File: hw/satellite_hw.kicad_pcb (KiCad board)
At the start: 2 copper layers, 17 parts, among them Q1 2N7002, U1 AP3015, U2 ATtiny13-20SU

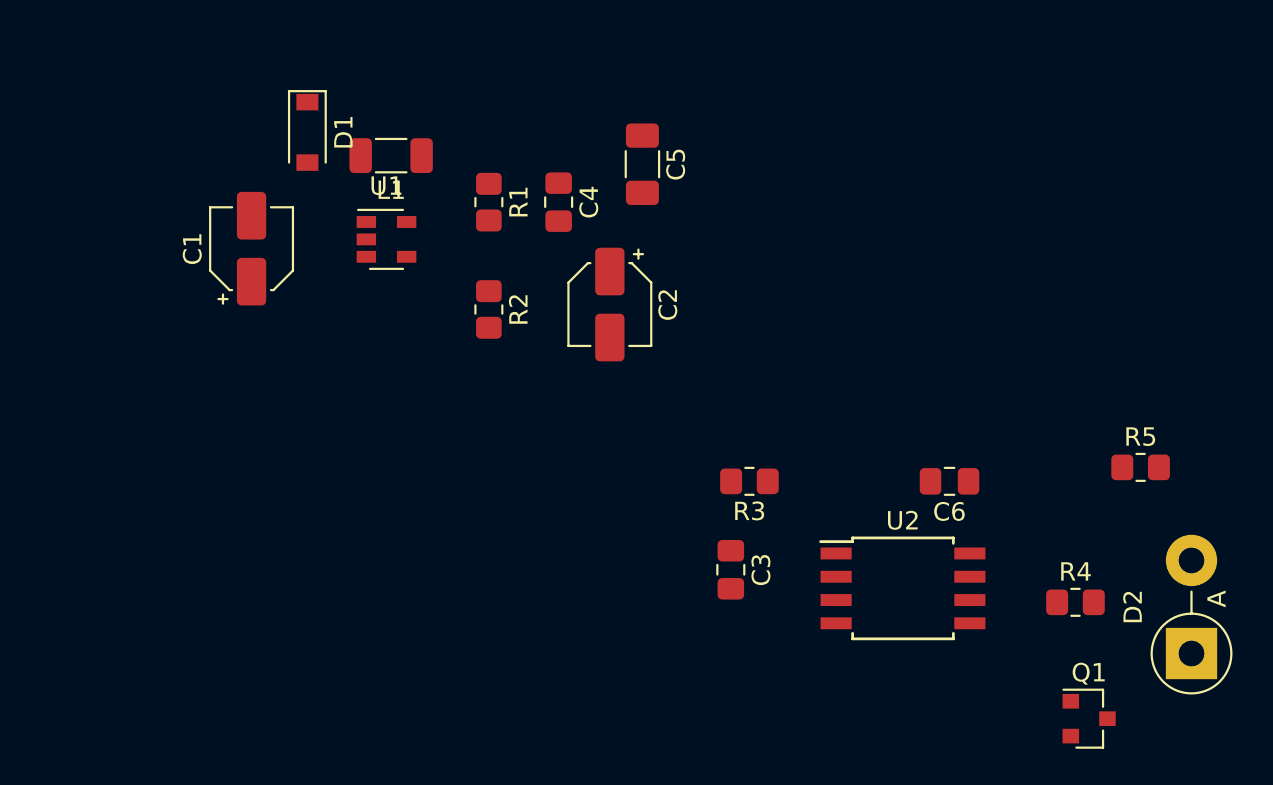
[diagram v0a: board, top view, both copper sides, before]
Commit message: PCB elements alignment + board ground layers
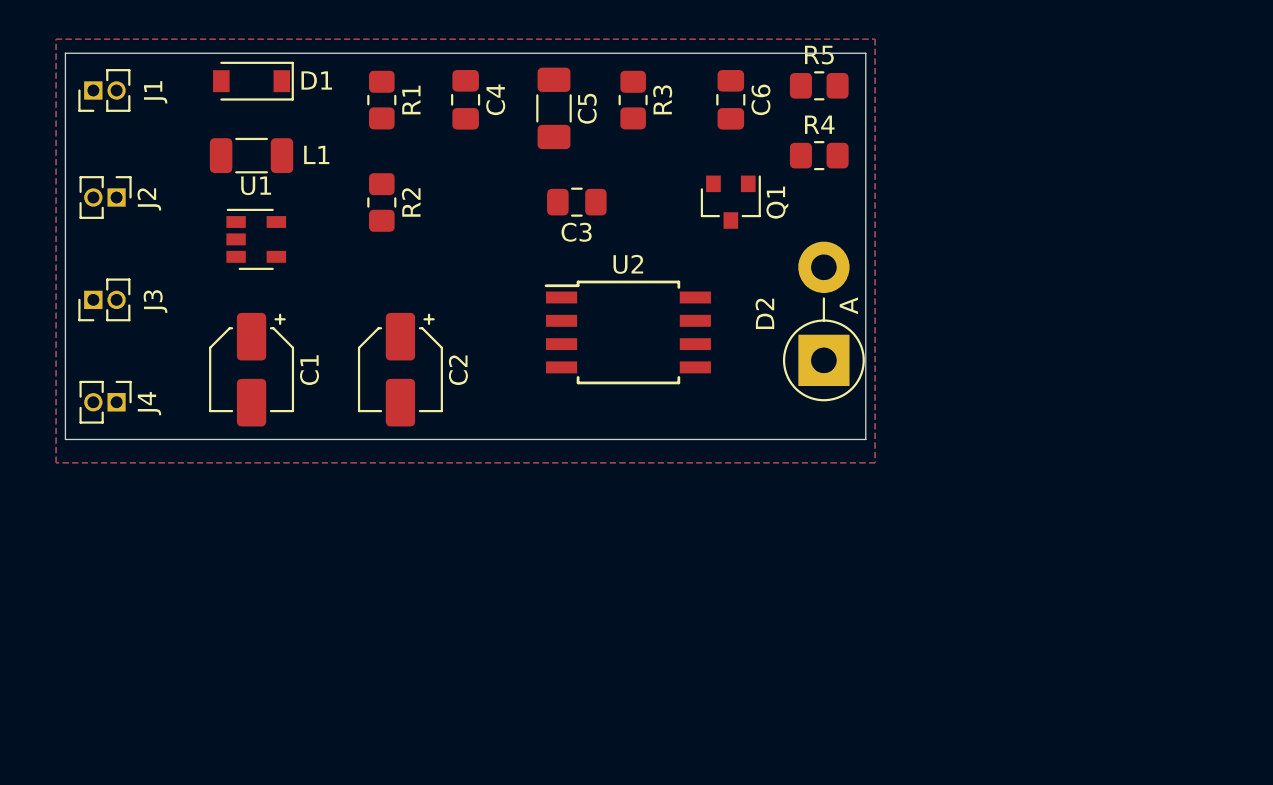
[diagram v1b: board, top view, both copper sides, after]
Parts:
- added J1: solar 1, Connector_PinHeader_1.27mm:PinHeader_1x02_P1.27mm_Vertical, F.Cu at (96.0, 74.7)
- added J2: solar 2, Connector_PinHeader_1.27mm:PinHeader_1x02_P1.27mm_Vertical, F.Cu at (97.3, 80.5)
- added J3: solar 3, Connector_PinHeader_1.27mm:PinHeader_1x02_P1.27mm_Vertical, F.Cu at (96.0, 86.1)
- added J4: solar 4, Connector_PinHeader_1.27mm:PinHeader_1x02_P1.27mm_Vertical, F.Cu at (97.3, 91.7)
- moved Q1 34.3 mm to (130.8, 80.8), turned to 270 degrees
- moved R4 28.1 mm to (135.6, 78.2)
- moved R5 27.2 mm to (135.6, 74.4)
- moved D2 25.7 mm to (135.9, 89.4)
- moved C6 24.0 mm to (130.8, 75.2), turned to 270 degrees
- moved R3 21.8 mm to (125.5, 75.2), turned to 270 degrees
- moved C3 21.8 mm to (122.4, 80.8), turned to 180 degrees
- moved U2 20.5 mm to (125.2, 87.9)
- moved C2 12.0 mm to (112.8, 89.9)
- moved R2 8.26 mm to (111.8, 80.8)
- moved R1 8.07 mm to (111.8, 75.2)
- moved L1 7.62 mm to (104.6, 78.2)
- moved C4 7.55 mm to (116.3, 75.2)
- moved U1 7.11 mm to (104.9, 82.8)
- moved C1 6.60 mm to (104.6, 89.9), turned to 270 degrees
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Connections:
- U2 pad 3: Net-(Q1-Pad1) -> Net-(U2-Pad3)
- U2 pad 6: Net-(U2-Pad6) -> Net-(Q1-Pad1)
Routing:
- added copper zone on B.Cu, net GNDD
- added copper zone on F.Cu, net GNDD
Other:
- board outline added: 43.7 x 21.1 mm

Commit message: removed bottom layer
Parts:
- moved C6 0.80 mm to (130.0, 75.4)
- moved Q1 0.36 mm to (130.6, 81.0), turned to 90 degrees
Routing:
- net +5V: track 0.00 -> 63.5 mm
- net Net-(C4-Pad2): track 0.00 -> 30.8 mm
- net VCC: track 0.00 -> 24.2 mm
- net Net-(Q1-Pad1): track 0.00 -> 21.5 mm
- net Net-(D2-Pad1): track 0.00 -> 13.3 mm
- net Net-(C3-Pad1): track 0.00 -> 11.4 mm
- net Net-(D2-Pad2): track 0.00 -> 11.2 mm
- net Net-(D1-Pad2): track 0.00 -> 8.03 mm
- net Net-(J1-Pad1): track 0.00 -> 5.84 mm
- net Net-(J3-Pad1): track 0.00 -> 5.59 mm
- net Net-(J2-Pad1): track 0.00 -> 5.59 mm
- net GNDD: track 0.00 -> 1.69 mm
- removed copper zone on B.Cu, net GNDD
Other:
- board text added: "+"
- board text added: "-"
- board text added: "toy satellite v0.1"

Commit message: fixed holdpin size
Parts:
- D2: footprint Diode_THT:D_5W_P5.08mm_Vertical_AnodeUp -> LED_THT:LED_D5.0mm-3
- J1, J2, J3, J4: footprint Connector_PinHeader_1.27mm:PinHeader_1x02_P1.27mm_Vertical -> Connector_PinHeader_2.00mm:PinHeader_1x02_P2.00mm_Vertical
- moved J2 0.76 mm to (98.0, 80.5)
- moved J4 0.76 mm to (98.0, 91.7)
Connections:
- U2 pad 2: Net-(U2-Pad2) -> (no net)
- U2 pad 3: Net-(U2-Pad3) -> (no net)
- U2 pad 5: Net-(U2-Pad5) -> (no net)
- U2 pad 7: Net-(U2-Pad7) -> (no net)
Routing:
- net VCC: track 24.2 -> 23.4 mm

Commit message: fixed THT LED size and pins
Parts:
- D2: footprint LED_THT:LED_D5.0mm-3 -> LED_THT:LED_D3.0mm
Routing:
- net Net-(D2-Pad2): track 11.2 -> 14.0 mm
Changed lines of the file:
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@@
     (thickness 1.6)
     (drawings 7)
-    (tracks 88)
+    (tracks 90)
     (zones 0)
     (modules 21)
@@
     (add_net VCC)
   )
+  (module LED_THT:LED_D3.0mm (layer F.Cu)
+    (at 135.89 89.408 90)
+    (descr "LED, diameter 3.0mm, 2 pins")
+    (tags "LED diameter 3.0mm 2 pins")
+    (fp_text reference D2 (at 1.27 -2.96 90) (layer F.SilkS)
+      (effects (font (size 1 1) (thickness 0.15)))
+    )
+    (fp_text value red (at 1.27 2.96 90) (layer F.Fab)
+      (effects (font (size 1 1) (thickness 0.15)))
+    )
+    (fp_arc (start 1.27 0) (end 0.229039 1.08) (angle -87.9) (layer F.SilkS) (width 0.12))
+    (fp_arc (start 1.27 0) (end 0.229039 -1.08) (angle 87.9) (layer F.SilkS) (width 0.12))
+    (fp_arc (start 1.27 0) (end -0.29 1.235516) (angle -108.8) (layer F.SilkS) (width 0.12))
+    (fp_arc (start 1.27 0) (end -0.29 -1.235516) (angle 108.8) (layer F.SilkS) (width 0.12))
+    (fp_arc (start 1.27 0) (end -0.23 -1.16619) (angle 284.3) (layer F.Fab) (width 0.1))
+    (fp_circle (center 1.27 0) (end 2.77 0) (layer F.Fab) (width 0.1))
+    (fp_line (start -0.23 -1.16619) (end -0.23 1.16619) (layer F.Fab) (width 0.1))
+    (fp_line (start -0.29 -1.236) (end -0.29 -1.08) (layer F.SilkS) (width 0.12))
+    (fp_line (start -0.29 1.08) (end -0.29 1.236) (layer F.SilkS) (width 0.12))
+    (fp_line (start -1.15 -2.25) (end -1.15 2.25) (layer F.CrtYd) (width 0.05))
+    (fp_line (start -1.15 2.25) (end 3.7 2.25) (layer F.CrtYd) (width 0.05))
+    (fp_line (start 3.7 2.25) (end 3.7 -2.25) (layer F.CrtYd) (width 0.05))
+    (fp_line (start 3.7 -2.25) (end -1.15 -2.25) (layer F.CrtYd) (width 0.05))
+    (pad 2 thru_hole circle (at 2.54 0 90) (size 1.8 1.8) (drill 0.9) (layers *.Cu *.Mask)
+      (net 8 "Net-(D2-Pad2)"))
+    (pad 1 thru_hole rect (at 0 0 90) (size 1.8 1.8) (drill 0.9) (layers *.Cu *.Mask)
+      (net 7 "Net-(D2-Pad1)"))
+    (model ${KISYS3DMOD}/LED_THT.3dshapes/LED_D3.0mm.wrl
+      (at (xyz 0 0 0))
+      (scale (xyz 1 1 1))
+      (rotate (xyz 0 0 0))
+    )
+  )
   (module Connector_PinHeader_2.00mm:PinHeader_1x02_P2.00mm_Vertical (layer F.Cu)
     (at 98.044 91.694 270)
@@
       (net 7 "Net-(D2-Pad1)"))
     (model ${KISYS3DMOD}/Package_TO_SOT_SMD.3dshapes/SOT-23.wrl
-      (at (xyz 0 0 0))
-      (scale (xyz 1 1 1))
-      (rotate (xyz 0 0 0))
-    )
-  )
-  (module LED_THT:LED_D5.0mm-3 (layer F.Cu)
-    (at 135.89 89.408 90)
-    (descr "LED, diameter 5.0mm, 2 pins, diameter 5.0mm, 3 pins, http://www.kingbright.com/attachments/file/psearch/000/00/00/L-59EGC(Ver.17A).pdf")
-    (tags "LED diameter 5.0mm 2 pins diameter 5.0mm 3 pins")
-    (fp_text reference D2 (at 2.54 -3.96 90) (layer F.SilkS)
-      (effects (font (size 1 1) (thickness 0.15)))
-    )
-    (fp_text value red (at 2.54 3.96 90) (layer F.Fab)
-      (effects (font (size 1 1) (thickness 0.15)))
-    )
-    (fp_line (start 6.25 -3.25) (end -1.15 -3.25) (layer F.CrtYd) (width 0.05))
-    (fp_line (start 6.25 3.25) (end 6.25 -3.25) (layer F.CrtYd) (width 0.05))
-    (fp_line (start -1.15 3.25) (end 6.25 3.25) (layer F.CrtYd) (width 0.05))
-    (fp_line (start -1.15 -3.25) (end -1.15 3.25) (layer F.CrtYd) (width 0.05))
-    (fp_line (start -0.02 1.08) (end -0.02 1.545) (layer F.SilkS) (width 0.12))
-    (fp_line (start -0.02 -1.545) (end -0.02 -1.08) (layer F.SilkS) (width 0.12))
-    (fp_line (start 0.04 -1.469694) (end 0.04 1.469694) (layer F.Fab) (width 0.1))
-    (fp_circle (center 2.54 0) (end 5.04 0) (layer F.Fab) (width 0.1))
-    (fp_arc (start 2.54 0) (end 0.04 -1.469694) (angle 299.1) (layer F.Fab) (width 0.1))
-    (fp_arc (start 2.54 0) (end -0.02 -1.54483) (angle 127.7) (layer F.SilkS) (width 0.12))
-    (fp_arc (start 2.54 0) (end -0.02 1.54483) (angle -127.7) (layer F.SilkS) (width 0.12))
-    (fp_arc (start 2.54 0) (end 0.285316 -1.08) (angle 128.8) (layer F.SilkS) (width 0.12))
-    (fp_arc (start 2.54 0) (end 0.285316 1.08) (angle -128.8) (layer F.SilkS) (width 0.12))
-    (pad 1 thru_hole rect (at 0 0 90) (size 1.8 1.8) (drill 0.9) (layers *.Cu *.Mask)
-      (net 7 "Net-(D2-Pad1)"))
-    (pad 2 thru_hole circle (at 2.54 0 90) (size 1.8 1.8) (drill 0.9) (layers *.Cu *.Mask)
-      (net 8 "Net-(D2-Pad2)"))
-    (pad 3 thru_hole circle (at 5.08 0 90) (size 1.8 1.8) (drill 0.9) (layers *.Cu *.Mask))
-    (model ${KISYS3DMOD}/LED_THT.3dshapes/LED_D5.0mm-3.wrl
       (at (xyz 0 0 0))
       (scale (xyz 1 1 1))
@@
   (segment (start 133.35 86.868) (end 135.89 89.408) (width 0.25) (layer F.Cu) (net 7))
   (segment (start 133.35 81.28) (end 133.35 86.868) (width 0.25) (layer F.Cu) (net 7))
-  (segment (start 135.89 84.328) (end 135.89 81.788) (width 0.25) (layer F.Cu) (net 8))
   (segment (start 135.89 81.788) (end 137.82599 79.85201) (width 0.25) (layer F.Cu) (net 8))
   (segment (start 137.82599 75.61199) (end 136.636 74.422) (width 0.25) (layer F.Cu) (net 8))
   (segment (start 137.82599 79.85201) (end 137.82599 75.61199) (width 0.25) (layer F.Cu) (net 8))
+  (segment (start 135.89 86.868) (end 135.89 84.074) (width 0.25) (layer F.Cu) (net 8))
+  (segment (start 135.89 84.074) (end 135.89 81.788) (width 0.25) (layer F.Cu) (net 8))
+  (segment (start 135.89 84.328) (end 135.89 84.074) (width 0.25) (layer F.Cu) (net 8))
   (segment (start 128.872 88.519) (end 130.429 88.519) (width 0.25) (layer F.Cu) (net 9))
   (segment (start 130.429 88.519) (end 130.81 88.138) (width 0.25) (layer F.Cu) (net 9))
